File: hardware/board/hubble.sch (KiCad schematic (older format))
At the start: 6 parts, among them J4 EXT, J5 Left, J6 Right, J7 Bottom, J8 EXT, J9 EXT

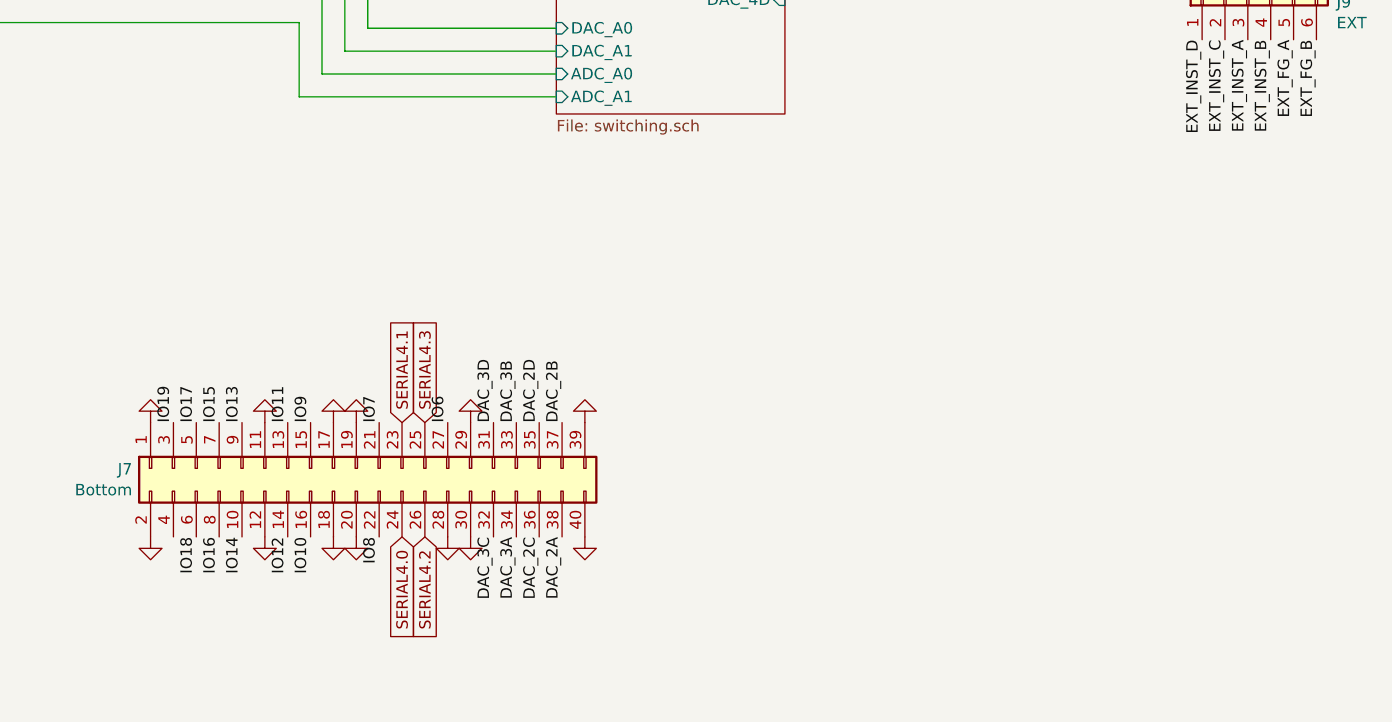
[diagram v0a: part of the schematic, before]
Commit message: More updates to the board design
- Added polyfuses for downstream power
- Added breakout header for external, panel-mounted USB port
- Added I/O breakout for the switches and buttons on the front control panel
- Made the MCU footprint a hybrid QFP/QFN footprint
- Add a nice illustration to the board backside
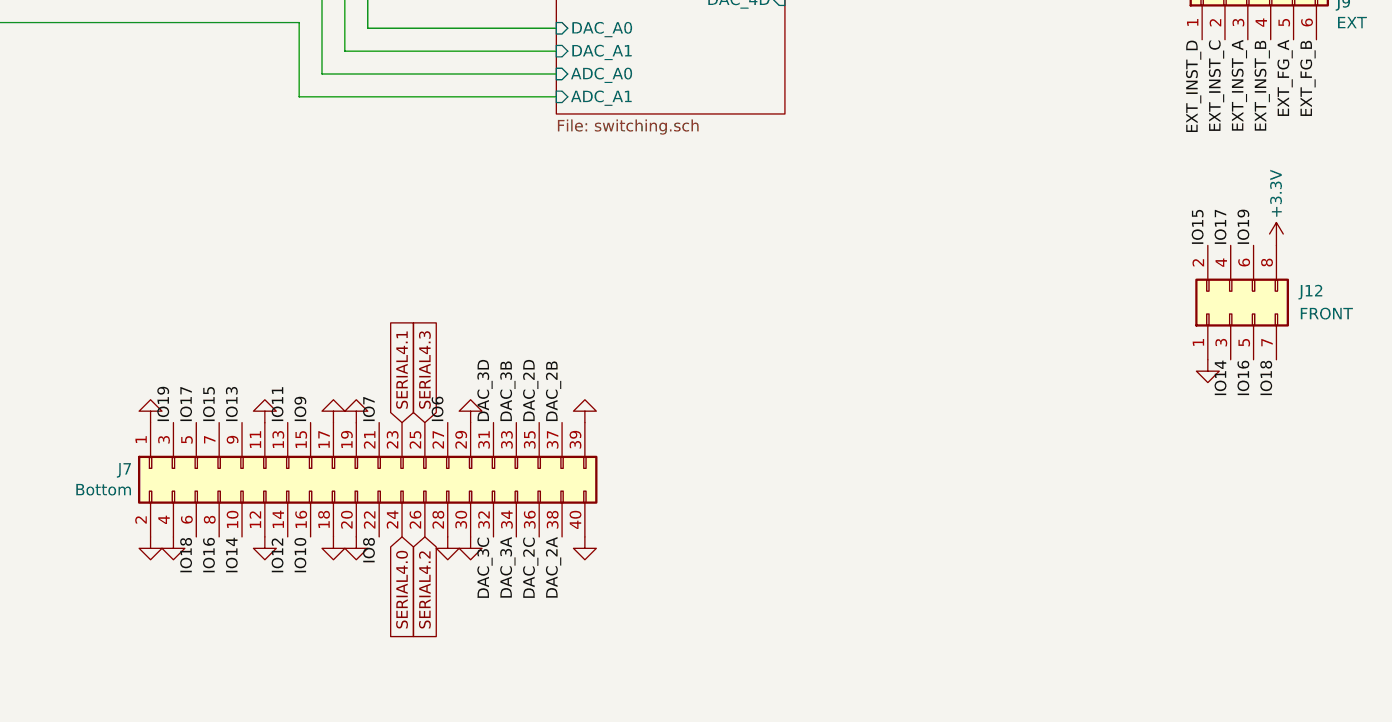
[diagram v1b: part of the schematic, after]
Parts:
- added J12: FRONT, Connector_PinHeader_2.54mm:PinHeader_2x04_P2.54mm_Vertical, symbol Connector_Generic:Conn_02x04_Odd_Even
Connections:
- net +3V3: now also J12.8 (Pin_8)
- net GND: now also J7.4 (Pin_4), J12.1 (Pin_1)
- net IO14: now also J12.3 (Pin_3)
- net IO15: now also J12.2 (Pin_2)
- net IO16: now also J12.5 (Pin_5)
- net IO17: now also J12.4 (Pin_4)
- net IO18: now also J12.7 (Pin_7)
- net IO19: now also J12.6 (Pin_6)
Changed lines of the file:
@@
 Sheet 1 7
 Title "Hubble Motherboard"
-Date "2021-11-12"
+Date "2021-11-20"
 Rev "v2"
 Comp "Winterbloom"
 Comment1 "Alethea Flowers"
 Comment2 "CERN-OHL-P V2"
-Comment3 ""
+Comment3 "hubble.wntr.dev"
 Comment4 ""
 $EndDescr
@@
 Wire Wire Line
 	3450 2950 2300 2950
+$Comp
+L Connector_Generic:Conn_02x04_Odd_Even J?
+U 1 1 619E345F
+P 9625 5375
+AR Path="/60711259/619E345F" Ref="J?"  Part="1"
+AR Path="/619E345F" Ref="J12"  Part="1"
+F 0 "J12" V 9725 5075 50  0000 R CNN
+F 1 "FRONT" V 9625 5075 50  0000 R CNN
+F 2 "Connector_PinHeader_2.54mm:PinHeader_2x04_P2.54mm_Vertical" H 9625 5375 50  0001 C CNN
+F 3 "~" H 9625 5375 50  0001 C CNN
+	1    9625 5375
+	0    -1   -1   0
+$EndComp
+$Comp
+L power:GND #PWR0220
+U 1 1 619EF9B6
+P 9525 5575
+F 0 "#PWR0220" H 9525 5325 50  0001 C CNN
+F 1 "GND" V 9530 5447 50  0001 R CNN
+F 2 "" H 9525 5575 50  0001 C CNN
+F 3 "" H 9525 5575 50  0001 C CNN
+	1    9525 5575
+	1    0    0    -1
+$EndComp
+Text Label 9525 5075 1    50   ~ 0
+IO15
+Text Label 9625 5075 1    50   ~ 0
+IO17
+Text Label 9725 5075 1    50   ~ 0
+IO19
+Text Label 9725 5575 3    50   ~ 0
+IO16
+Text Label 9825 5575 3    50   ~ 0
+IO18
+$Comp
+L power:GND #PWR0221
+U 1 1 619F674A
+P 5000 6350
+F 0 "#PWR0221" H 5000 6100 50  0001 C CNN
+F 1 "GND" H 5005 6177 50  0001 C CNN
+F 2 "" H 5000 6350 50  0001 C CNN
+F 3 "" H 5000 6350 50  0001 C CNN
+	1    5000 6350
+	1    0    0    -1
+$EndComp
+Text Label 9625 5575 3    50   ~ 0
+IO14
+$Comp
+L power:+3.3V #PWR?
+U 1 1 619F9149
+P 9825 5075
+AR Path="/60711259/619F9149" Ref="#PWR?"  Part="1"
+AR Path="/619F9149" Ref="#PWR0222"  Part="1"
+F 0 "#PWR0222" H 9825 4925 50  0001 C CNN
+F 1 "+3.3V" V 9825 5300 50  0000 C CNN
+F 2 "" H 9825 5075 50  0001 C CNN
+F 3 "" H 9825 5075 50  0001 C CNN
+	1    9825 5075
+	-1   0    0    -1
+$EndComp
 $EndSCHEMATC
